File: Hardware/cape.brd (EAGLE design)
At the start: 123 x 126 mm, 40 parts, among them IC1 74VHC541, IC2 74VHC541, IC3 74VHC541, IC4 74VHC541, IC5 74VHC541, IC6 74VHC541, IC7 74VHC541, J3 RJ45-8P8C, Q1 N-MOSFET-DUALSO8, Q10 N-MOSFET-DUALSO8, Q11 N-MOSFET-DUALSO8, Q12 N-MOSFET-DUALSO8, Q13 N-MOSFET-DUALSO8, Q14 N-MOSFET-DUALSO8, Q15 N-MOSFET-DUALSO8, Q16 N-MOSFET-DUALSO8, Q2 N-MOSFET-DUALSO8, Q3 N-MOSFET-DUALSO8, Q4 N-MOSFET-DUALSO8, Q5 N-MOSFET-DUALSO8, Q6 N-MOSFET-DUALSO8, Q7 N-MOSFET-DUALSO8, Q8 N-MOSFET-DUALSO8, Q9 N-MOSFET-DUALSO8

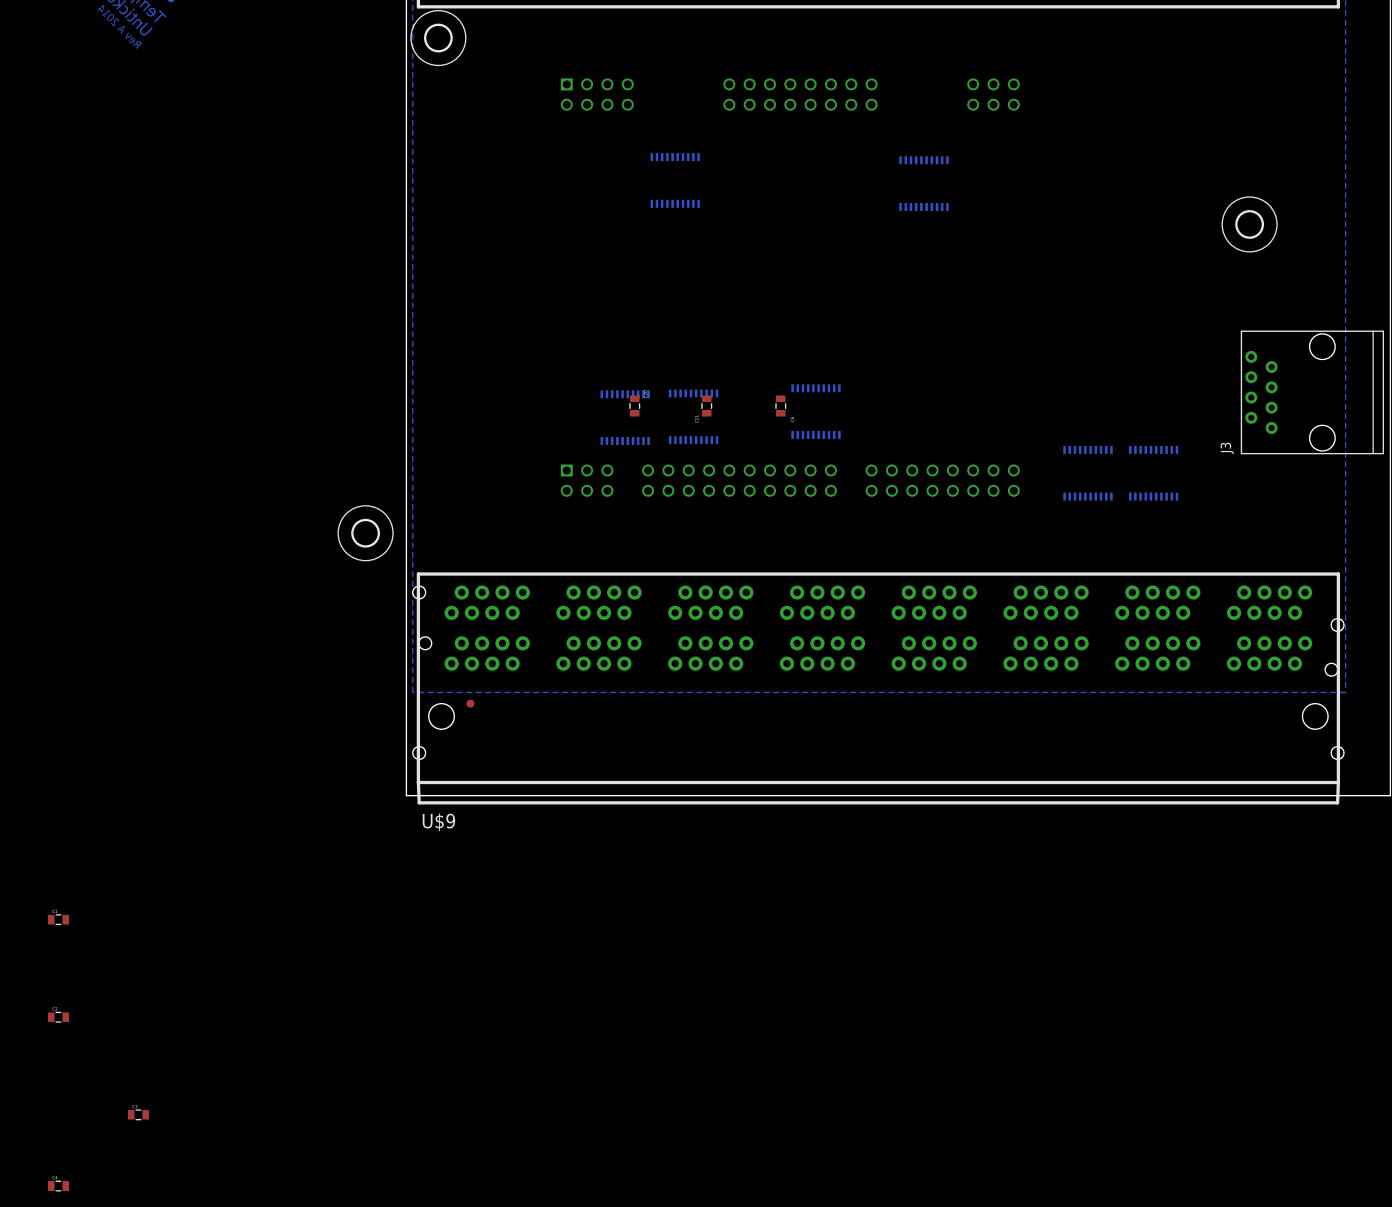
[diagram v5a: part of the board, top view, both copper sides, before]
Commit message: Buffer all the things
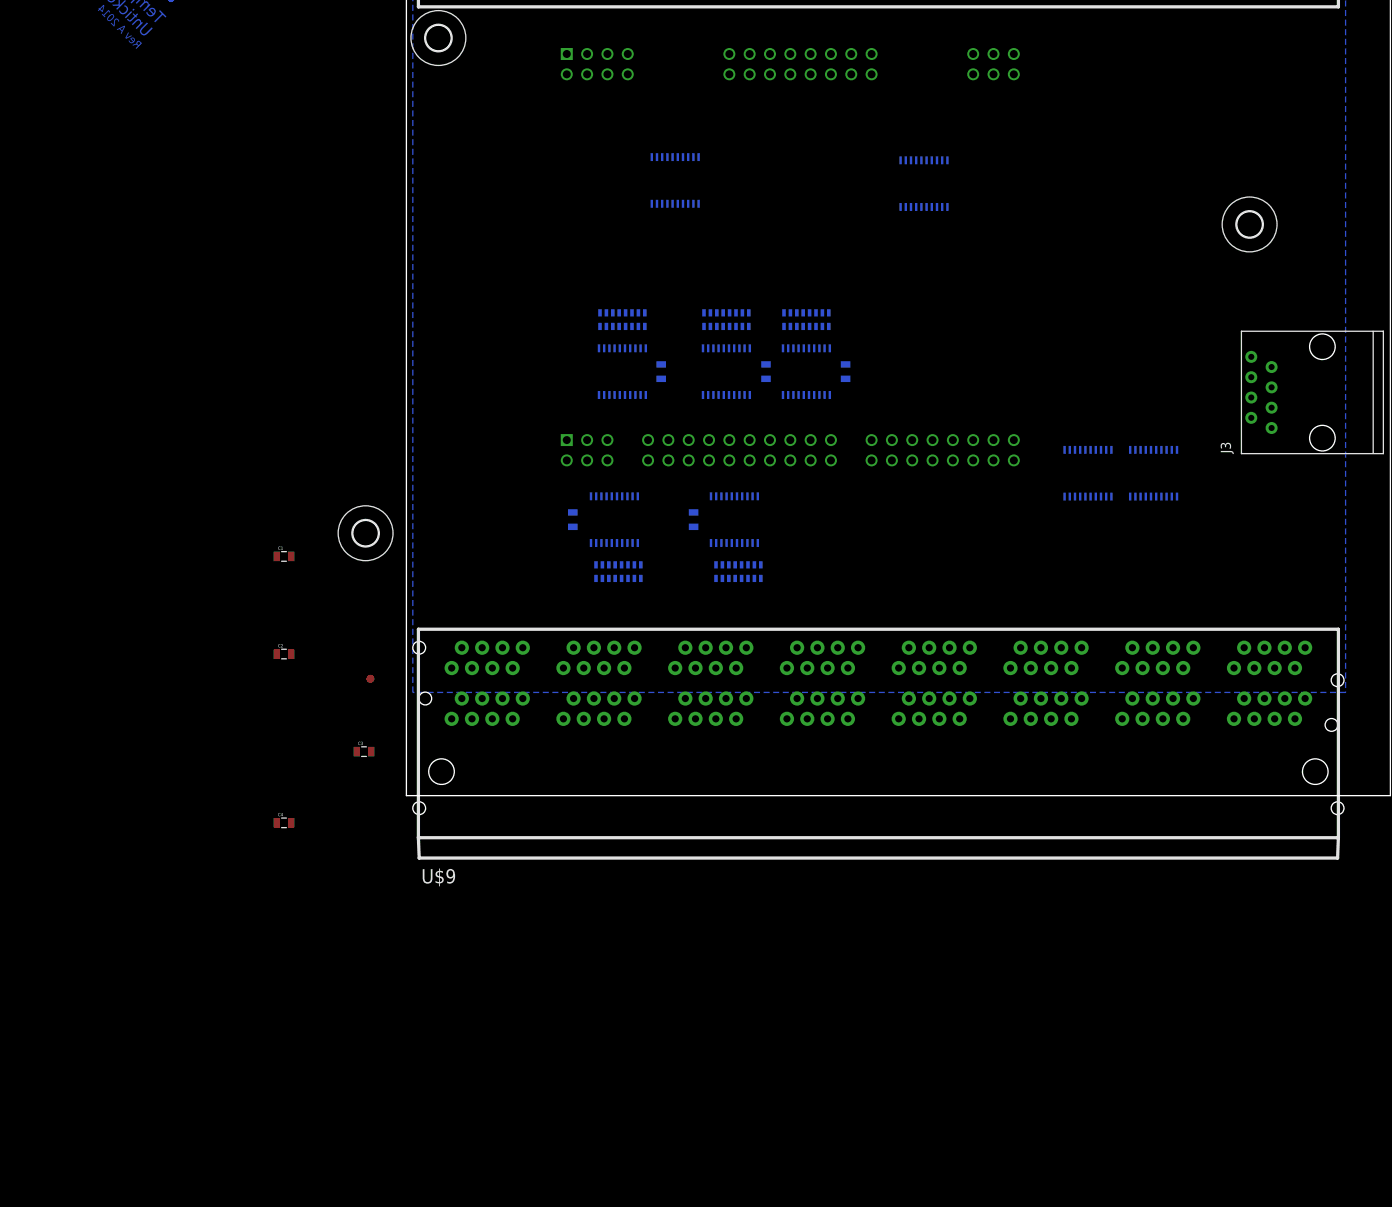
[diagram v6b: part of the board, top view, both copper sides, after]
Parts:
- added C5, C7: 1uF, SparkFun-Capacitors:0805
- added IC8, IC9: 74VHC541, cape:TSSOP20
- added R1, R2, R3, R4, R5: RESISTOR-X80603, cape:R0603-X8
- moved C1 53.4 mm to (-15.3, 21.9)
- moved C3 53.4 mm to (-5.30, -2.50)
- moved C4 53.4 mm to (-15.3, -11.4)
- moved C2 53.4 mm to (-15.3, 9.70)
- moved U$5 12.9 mm to (-4.50, 6.60)
- moved C6 9.17 mm to (54.9, 45.0), flipped to the bottom
- moved C21 8.56 mm to (45.0, 45.0), flipped to the bottom
- moved IC5 6.98 mm to (40.0, 45.0)
- moved U$9 6.90 mm to (59.0, -5.00)
- moved IC4 5.76 mm to (27.0, 45.0)
- moved C20 5.42 mm to (31.9, 45.0), flipped to the bottom
- moved IC2 5.14 mm to (50.0, 45.0)
- moved U$1 3.80 mm to (1.00, 32.0)
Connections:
- removed net BUF0: IC5.11
- removed net BUF1: IC5.12
- removed net BUF10: IC4.11
- removed net BUF11: IC5.16
- removed net BUF12: IC4.13
- removed net BUF13: IC4.14
- removed net BUF14: IC5.17
- removed net BUF15: IC5.18
- removed net BUF2: IC4.16
- removed net BUF3: IC4.15
- removed net BUF4: IC5.13
- removed net BUF5: IC5.14
- removed net BUF6: IC4.18
- removed net BUF7: IC4.17
- removed net BUF8: IC5.15
- removed net BUF9: IC4.12
- removed net DATA-10-1: U$9.LH1
- removed net DATA-10-2: U$9.UH1
- removed net DATA-12-1: U$9.LF1
- removed net DATA-12-2: U$9.UF1
- removed net DATA-13-1: U$9.LE1
- removed net DATA-13-2: U$9.UE1
- removed net DATA-2-1: U$9.LC1
- removed net DATA-2-2: U$9.UC1
- removed net DATA-3-1: U$9.LD1
- removed net DATA-3-2: U$9.UD1
- removed net DATA-6-1: U$9.LA1
- removed net DATA-6-2: U$9.UA1
- removed net DATA-7-1: U$9.LB1
- removed net DATA-7-2: U$9.UB1
- removed net DATA-9-1: U$9.LG1
- removed net DATA-9-2: U$9.UG1
- removed net SCL_BUF_1: IC1.2, IC2.18, IC3.2
- removed net SCL_BUF_2: IC2.17, IC6.2, IC7.2
- new net BUF0_A: R5.7A
- new net BUF0_B: R2.8A, U$9.LH1
- new net BUF10_A: R4.7A
- new net BUF10_B: R1.8A, U$9.LD1
- new net BUF11_A: R4.4A
- new net BUF11_B: R2.3A, U$9.UF1
- new net BUF12_A: R3.2A
- new net BUF12_B: R1.6A, U$9.LC1
- new net BUF13_A: R3.1A
- new net BUF13_B: R1.5A, U$9.UC1
- new net BUF14_A: R4.5A
- new net BUF14_B: R2.1A, U$9.UE1
- new net BUF15_A: R4.6A
- new net BUF15_B: R2.2A, U$9.LE1
- new net BUF1_A: R5.8A
- new net BUF1_B: R2.7A, U$9.UH1
- new net BUF2_A: R3.6A
- new net BUF2_B: R1.3A, U$9.UB1
- new net BUF3_A: R3.5A
- new net BUF3_B: R1.4A, U$9.LB1
- new net BUF4_A: R4.1A
- new net BUF4_B: R2.6A, U$9.LG1
- new net BUF5_A: R4.2A
- new net BUF5_B: R2.5A, U$9.UG1
- new net BUF6_A: R3.8A
- new net BUF6_B: R1.1A, U$9.UA1
- new net BUF7_A: R3.7A
- new net BUF7_B: R1.2A, U$9.LA1
- new net BUF8_A: R4.3A
- new net BUF8_B: R2.4A, U$9.LF1
- new net BUF9_A: R4.8A
- new net BUF9_B: R1.7A, U$9.UD1
- new net N$1: IC2.2
- new net N$10: IC8.15, R1.4B
- new net N$11: IC8.14, R1.5B
- new net N$12: IC8.13, R1.6B
- new net N$13: IC8.12, R1.7B
- new net N$14: IC8.11, R1.8B
- new net N$15: IC9.18, R2.1B
- new net N$16: IC9.17, R2.2B
- new net N$17: IC9.16, R2.3B
- new net N$18: IC9.15, R2.4B
- new net N$19: IC9.14, R2.5B
- new net N$2: IC2.3
- new net N$20: IC9.13, R2.6B
- new net N$21: IC9.12, R2.7B
- new net N$22: IC9.11, R2.8B
- new net N$23: IC5.18, R4.1B
- new net N$24: IC5.17, R4.2B
- new net N$25: IC5.16, R4.3B
- new net N$26: IC5.15, R4.4B
- new net N$27: IC5.13, R4.6B
- new net N$28: IC5.14, R4.5B
- new net N$29: IC5.12, R4.7B
- new net N$3: IC2.4
- new net N$30: IC5.11, R4.8B
- new net N$31: IC4.18, R3.1B
- new net N$32: IC4.17, R3.2B
- new net N$34: IC2.12, R5.7B
- new net N$35: IC4.14, R3.5B
- new net N$36: IC4.13, R3.6B
- new net N$37: IC4.12, R3.7B
- new net N$38: IC4.11, R3.8B
- new net N$39: IC2.11, R5.8B
- new net N$4: IC2.5
- new net N$5: IC2.6
- new net N$6: IC2.7
- new net N$7: IC8.18, R1.1B
- new net N$8: IC8.17, R1.2B
- new net N$9: IC8.16, R1.3B
- new net SCL_BUF_A: IC1.2, IC1.3, IC1.4, IC1.5, IC1.6, IC1.7, IC1.8, IC1.9, IC3.2, IC3.3, IC3.4, IC3.5, IC3.6, IC3.7, IC3.8, IC3.9, IC4.16
- new net SCL_BUF_B: IC4.15, IC6.2, IC6.3, IC6.4, IC6.5, IC6.6, IC6.7, IC6.8, IC6.9, IC7.2, IC7.3, IC7.4, IC7.5, IC7.6, IC7.7, IC7.8, IC7.9
- net AD0: now also IC2.8, IC9.9; no longer IC5.9
- net AD1: now also IC2.9, IC9.8; no longer IC5.8
- net AD10: now also IC5.8, IC8.9; no longer IC4.9
- net AD11: now also IC5.5, IC9.4; no longer IC5.4
- net AD12: now also IC4.3, IC8.7; no longer IC4.7
- net AD13: now also IC4.2, IC8.6; no longer IC4.6
- net AD14: now also IC5.6, IC9.2; no longer IC5.3
- net AD15: now also IC5.7, IC9.3; no longer IC5.2
- net AD2: now also IC4.7, IC8.4; no longer IC4.4
- net AD3: now also IC4.6, IC8.5; no longer IC4.5
- net AD4: now also IC5.2, IC9.7; no longer IC5.7
- net AD5: now also IC5.3, IC9.6; no longer IC5.6
- net AD6: now also IC4.9, IC8.2; no longer IC4.2
- net AD7: now also IC4.8, IC8.3; no longer IC4.3
- net AD8: now also IC5.4, IC9.5; no longer IC5.5
- net AD9: now also IC5.9, IC8.8; no longer IC4.8
- net GND: now also C5.2, C7.2, IC8.1, IC8.10, IC8.19, IC9.1, IC9.10, IC9.19
- net SCL_RAW: now also IC4.4, IC4.5; no longer IC2.2, IC2.3
- net VCC3V3: now also C5.1, C7.1, IC8.20, IC9.20

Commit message: Routing
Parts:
- added R6, R7: RESISTOR-X80603, cape:R0603-X8
- moved C2 101.8 mm to (67.5, 69.0), flipped to the bottom, turned to 270 degrees
- moved C4 93.0 mm to (71.2, 22.7), flipped to the bottom, turned to 270 degrees
- moved C1 71.7 mm to (38.8, 69.0), flipped to the bottom, turned to 270 degrees
- moved C3 70.1 mm to (60.1, 22.7), flipped to the bottom, turned to 270 degrees
- moved IC6 21.1 mm to (64.9, 26.5)
- moved U$4 20.7 mm to (-11.3, 90.9)
- moved IC7 18.4 mm to (75.9, 26.5)
- moved U$10 6.60 mm to (59.0, 115.0)
- moved IC3 2.33 mm to (62.4, 68.9)
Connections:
- removed net DATA-0-1: U$10.UA1
- removed net DATA-0-2: U$10.LA1
- removed net DATA-1-1: U$10.UB1
- removed net DATA-1-2: U$10.LB1
- removed net DATA-11-1: U$10.UF1
- removed net DATA-11-2: U$10.LF1
- removed net DATA-14-1: U$10.UG1
- removed net DATA-14-2: U$10.LG1
- removed net DATA-15-1: U$10.UH1
- removed net DATA-15-2: U$10.LH1
- removed net DATA-4-1: U$10.UC1
- removed net DATA-4-2: U$10.LC1
- removed net DATA-5-1: U$10.UD1
- removed net DATA-5-2: U$10.LD1
- removed net DATA-8-1: U$10.UE1
- removed net DATA-8-2: U$10.LE1
- removed net SCL-A-1: U$9.LA8, U$9.LB8
- removed net SCL-A-2: U$9.UA8, U$9.UB8
- removed net SCL-B-1: U$9.LC8, U$9.LD8
- removed net SCL-B-2: U$9.UC8, U$9.UD8
- removed net SCL-C-1: U$9.LE8, U$9.LF8
- removed net SCL-C-2: U$9.UE8, U$9.UF8
- removed net SCL-D-1: U$9.LG8, U$9.LH8
- removed net SCL-D-2: U$9.UG8, U$9.UH8
- new net N$33: IC6.18, R6.1B
- new net N$40: IC6.17, R6.2B
- new net N$41: IC6.16, R6.3B
- new net N$42: IC6.15, R6.4B
- new net N$43: IC6.14, R6.5B
- new net N$44: IC6.13, R6.6B
- new net N$45: IC6.12, R6.7B
- new net N$46: IC6.11, R6.8B
- new net N$47: IC7.18, R7.1B
- new net N$48: IC7.17, R7.2B
- new net N$49: IC7.15, R7.4B
- new net N$50: IC7.16, R7.3B
- new net N$51: IC7.14, R7.5B
- new net N$52: IC7.12, R7.7B
- new net N$53: IC7.13, R7.6B
- new net N$54: IC7.11, R7.8B
- new net SCL0_B: R7.7A, U$9.UH8
- new net SCL10_B: R6.7A, U$9.UD8
- new net SCL11_B: R7.4A, U$9.LF8
- new net SCL12_B: R6.5A, U$9.UC8
- new net SCL13_B: R6.6A, U$9.LC8
- new net SCL14_B: R7.2A, U$9.LE8
- new net SCL15_B: R7.1A, U$9.UE8
- new net SCL1_B: R7.8A, U$9.LH8
- new net SCL2_B: R6.4A, U$9.LB8
- new net SCL3_B: R6.3A, U$9.UB8
- new net SCL4_B: R7.5A, U$9.UG8
- new net SCL5_B: R7.6A, U$9.LG8
- new net SCL6_B: R6.2A, U$9.LA8
- new net SCL7_B: R6.1A, U$9.UA8
- new net SCL8_B: R7.3A, U$9.UF8
- new net SCL9_B: R6.8A, U$9.LD8
- net 10A: no longer IC6.17, IC7.17
- net 11A: no longer IC6.16, IC7.16
- net 12A: no longer IC6.15, IC7.15
- net 13A: no longer IC6.14, IC7.14
- net 14A: no longer IC6.13, IC7.13
- net 15A: no longer IC6.12, IC7.12
- net 16A: no longer IC6.11, IC7.11
- net 9A: no longer IC6.18, IC7.18
- net AD12: now also IC4.2; no longer IC4.3
- net AD13: now also IC4.3; no longer IC4.2
- net AD14: now also IC5.7; no longer IC5.6
- net AD15: now also IC5.6; no longer IC5.7
- net BUF0_A: now also U$10.UA1
- net BUF0_B: now also U$9.LE1; no longer U$9.LH1
- net BUF10_A: now also U$10.UE1
- net BUF10_B: now also U$9.LA1; no longer U$9.LD1
- net BUF11_A: now also U$10.LC1
- net BUF11_B: now also U$9.UG1; no longer U$9.UF1
- net BUF12_A: now also R3.1A, U$10.UF1; no longer R3.2A
- net BUF12_B: now also U$9.LB1; no longer U$9.LC1
- net BUF13_A: now also R3.2A, U$10.LF1; no longer R3.1A
- net BUF13_B: now also U$9.UB1; no longer U$9.UC1
- net BUF14_A: now also R4.6A, U$10.UD1; no longer R4.5A
- net BUF14_B: now also U$9.UH1; no longer U$9.UE1
- net BUF15_A: now also R4.5A, U$10.LD1; no longer R4.6A
- net BUF15_B: now also U$9.LH1; no longer U$9.LE1
- net BUF1_A: now also U$10.LA1
- net BUF1_B: now also U$9.UE1; no longer U$9.UH1
- net BUF2_A: now also U$10.UG1
- net BUF2_B: now also U$9.UC1; no longer U$9.UB1
- net BUF3_A: now also U$10.LG1
- net BUF3_B: now also U$9.LC1; no longer U$9.LB1
- net BUF4_A: now also U$10.UB1
- net BUF4_B: now also U$9.LF1; no longer U$9.LG1
- net BUF5_A: now also U$10.LB1
- net BUF5_B: now also U$9.UF1; no longer U$9.UG1
- net BUF6_A: now also U$10.LH1
- net BUF6_B: now also U$9.UD1; no longer U$9.UA1
- net BUF7_A: now also U$10.UH1
- net BUF7_B: now also U$9.LD1; no longer U$9.LA1
- net BUF8_A: now also U$10.UC1
- net BUF8_B: now also U$9.LG1; no longer U$9.LF1
- net BUF9_A: now also U$10.LE1
- net BUF9_B: now also U$9.UA1; no longer U$9.UD1
- net VCC3V3: no longer C1.1, C2.1, C20.1, C21.1, C3.1, C4.1, C5.1, C6.1, C7.1, IC1.20, IC2.20, IC3.20, IC4.20, IC5.20, IC6.20, IC7.20, IC8.20, IC9.20
- net VCC5V: now also C1.1, C2.1, C20.1, C21.1, C3.1, C4.1, C5.1, C6.1, C7.1, IC1.20, IC2.20, IC3.20, IC4.20, IC5.20, IC6.20, IC7.20, IC8.20, IC9.20
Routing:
- net BUF1_B: track 0.00 -> 164.4 mm
- net BUF0_B: track 0.00 -> 162.8 mm
- net BUF4_B: track 0.00 -> 148.7 mm
- net BUF5_B: track 0.00 -> 147.1 mm
- net BUF8_B: track 0.00 -> 134.2 mm
- net BUF11_B: track 0.00 -> 129.1 mm
- net BUF15_B: track 0.00 -> 115.5 mm
- net BUF6_B: track 0.00 -> 113.5 mm
- net BUF2_B: track 0.00 -> 98.2 mm
- net BUF14_B: track 0.00 -> 94.2 mm
- net BUF7_B: track 0.00 -> 92.7 mm
- net BUF13_B: track 0.00 -> 83.2 mm
- net BUF3_B: track 0.00 -> 77.2 mm
- net SCL7_B: track 0.00 -> 66.9 mm
- net BUF9_B: track 0.00 -> 66.1 mm
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- removed copper zone on layer 16, net GND
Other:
- board size 123 x 126 mm -> 128 x 126 mm
